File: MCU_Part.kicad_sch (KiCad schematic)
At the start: 10 parts, among them U1 STM32G473RCTx

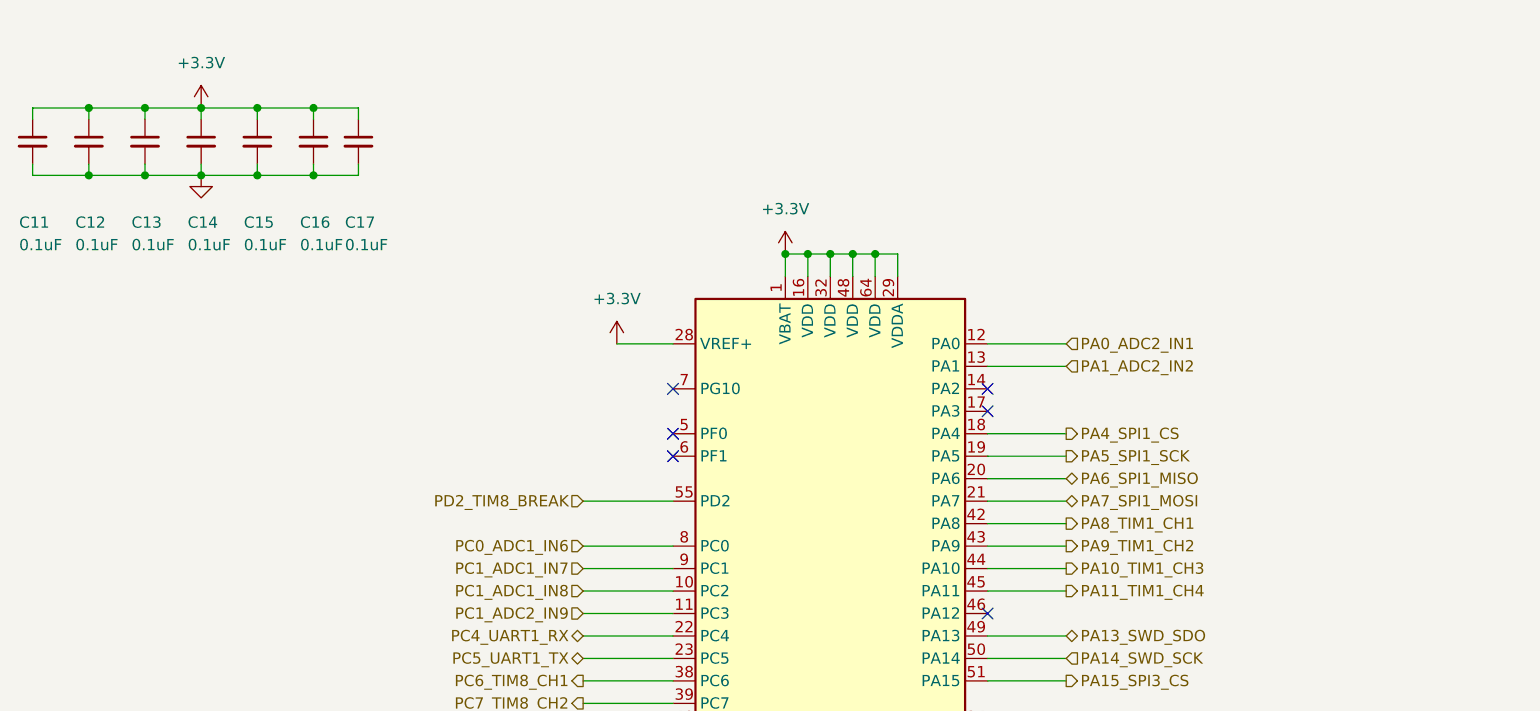
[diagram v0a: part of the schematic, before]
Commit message: 增加晶振电路
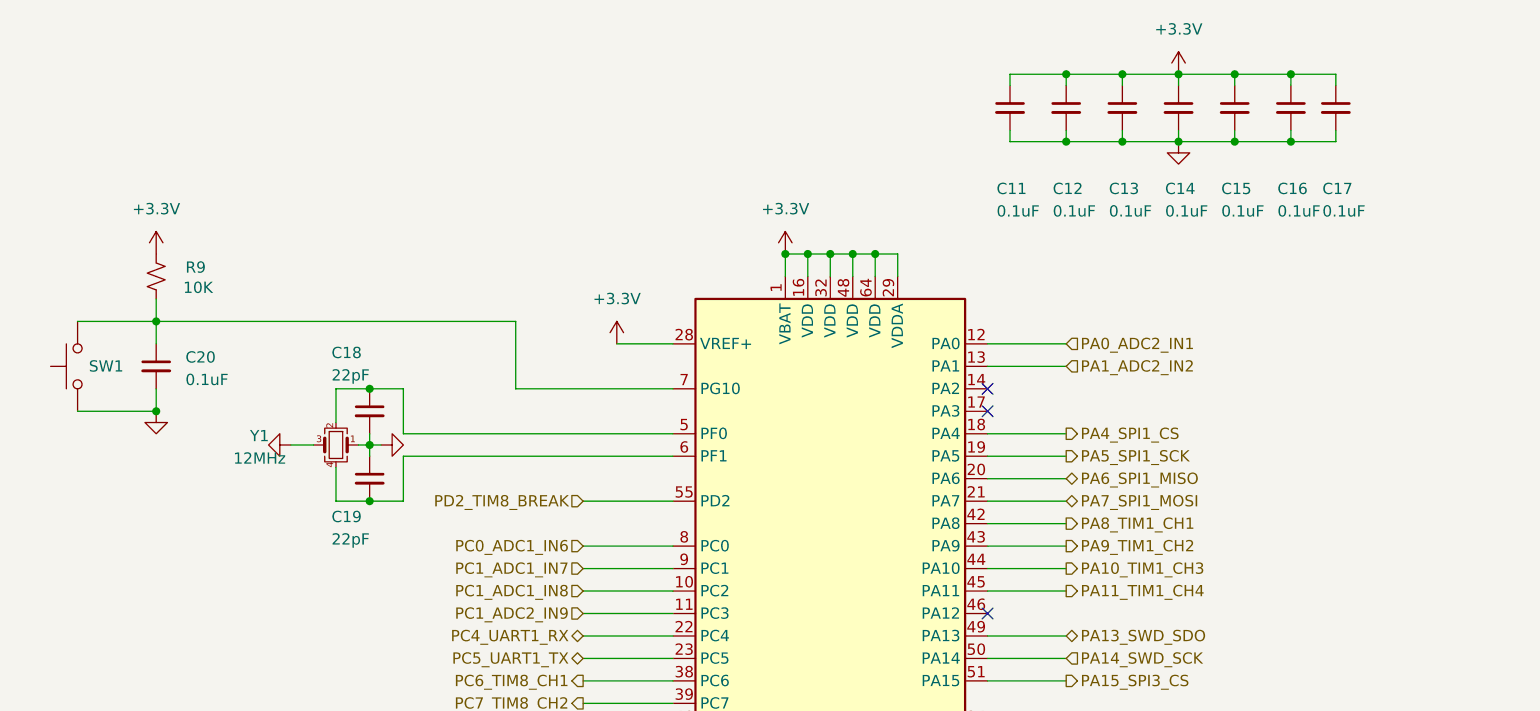
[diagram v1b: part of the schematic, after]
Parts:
- added C18, C19: 22pF, Capacitor_SMD:C_0603_1608Metric_Pad1.08x0.95mm_HandSolder, symbol Device:C_Small
- added C20: 0.1uF, Capacitor_SMD:C_0603_1608Metric_Pad1.08x0.95mm_HandSolder, symbol Device:C_Small
- added R9: 10K, Resistor_SMD:R_0603_1608Metric_Pad0.98x0.95mm_HandSolder, symbol Device:R_Small_US
- added SW1: SW_Push, symbol Switch:SW_Push
- added Y1: 12MHz, symbol Device:Crystal_GND24_Small
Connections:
- net +3.3V: now also R9.1
- net GND: now also C18.2, C19.1, C20.2, SW1.1, Y1.1, Y1.3
- net at U1.5 (PF0): now also C18.1, Y1.2
- net at U1.6 (PF1): now also C19.2, Y1.4
- net at U1.7 (PG10): now also C20.1, R9.2, SW1.2
- no-connect marks 11 -> 8
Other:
- moved on the sheet: C11, C12, C13, C14, C15, C16, C17

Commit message: PCB初布局
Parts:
- SW1: footprint (none) -> Button_Switch_SMD:SW_SPST_CK_RS282G05A3
- Y1: footprint (none) -> Crystal:Crystal_SMD_3225-4Pin_3.2x2.5mm
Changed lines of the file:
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@@
 			)
 		)
-		(property "Footprint" ""
+		(property "Footprint" "Crystal:Crystal_SMD_3225-4Pin_3.2x2.5mm"
 			(at 55.88 63.5 0)
 			(effects
@@
 			)
 		)
-		(property "Footprint" ""
+		(property "Footprint" "Button_Switch_SMD:SW_SPST_CK_RS282G05A3"
 			(at 21.59 54.61 0)
 			(effects

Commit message: 优化Type-C电路
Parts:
- Y1: value 12MHz -> 32MHz
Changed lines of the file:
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@@
 			)
 		)
-		(property "Value" "12MHz"
+		(property "Value" "32MHz"
 			(at 47.244 65.024 0)
 			(effects

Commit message: 优化布局20250919
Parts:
- added C21: 0.1uF, Capacitor_SMD:C_0603_1608Metric_Pad1.08x0.95mm_HandSolder, symbol Device:C_Small
- added R15: 10K, Resistor_SMD:R_0603_1608Metric_Pad0.98x0.95mm_HandSolder, symbol Device:R_Small_US
- added SW2: SW_Push, Button_Switch_SMD:SW_SPST_CK_RS282G05A3, symbol Switch:SW_Push
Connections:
- net +3.3V: now also R15.1
- net GND: now also C21.2, SW2.1
- net at U1.2 (PC13): now also C21.1, R15.2, SW2.2
- no-connect marks 8 -> 7
